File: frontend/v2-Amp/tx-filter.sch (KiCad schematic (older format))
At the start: 88 parts, among them K10 HK4100, K11 HK4100, K12 HK4100, K13 HK4100, K14 HK4100, K15 HK4100, K2 HK4100, K3 HK4100, K4 HK4100, K5 HK4100, K6 HK4100, K7 HK4100, K8 HK4100, K9 HK4100

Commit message: Starting V1.1 updates
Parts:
- added C2: 82pf, HERMESLITE:C_0805, symbol C
- added C3, C63: DNI, HERMESLITE:C_0805, symbol C
- added C4, C6: 150pf, HERMESLITE:C_0805, symbol C
- added C5: 56pf, HERMESLITE:C_0805, symbol C
- added C64: 82pF, HERMESLITE:C_0805, symbol C
- added L1, L22: 363nH, HERMESLITE:Choke_Toroid, symbol INDUCTOR
- added L2: 243nH, HERMESLITE:Choke_Toroid, symbol INDUCTOR
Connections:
- wire segments 147 -> 156
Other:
- note added: "11T T37-6\n7in #26"
- note added: "12/10M"
- note added: "12T T37-6\n8in #26"
- note added: "15T T37-6\n8in #26"
- note added: "16T T37-6\n9in #26"
- note added: "18T T37-6\n10in #26"
- note added: "19T T37-6\n11in #26"
- note added: "20T T37-6\n12in #26"
- note added: "23T T37-6\n13in #26"
- note added: "24T T37-2 \n14in #26"
- note added: "26T T37-2 \n15in #26"
- note added: "31T T37-2 \n17in #26"
- note added: "33T T37-2 \n18in #26"
- note added: "8T T37-6\n6in #26"
- note added: "9T T37-6\n7in #26"
- note removed: "12/10M and bypass"
- note removed: "12T T37-6\n #26"
- note removed: "14T T37-6\n #26"
- note removed: "16T T37-6\n #26"
- note removed: "17T T37-6\n #26"
- note removed: "19T T37-6\n #26"
- note removed: "20T T37-6\n #26"
- note removed: "21T T37-6\n #26"
- note removed: "25T T37-2 \n #28"
- note removed: "27T T37-2 \n #28"
- note removed: "30T T50-2 \n #30"
- note removed: "34T T50-2 \n #30"

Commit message: Filter updates
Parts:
- removed C2: 82pf, HERMESLITE:C_0805, symbol C
- removed C3, C63: DNI, HERMESLITE:C_0805, symbol C
- removed C4, C6: 150pf, HERMESLITE:C_0805, symbol C
- removed C5: 56pf, HERMESLITE:C_0805, symbol C
- removed C64: 82pF, HERMESLITE:C_0805, symbol C
- removed L1, L22: 363nH, HERMESLITE:Choke_Toroid, symbol INDUCTOR
- removed L2: 243nH, HERMESLITE:Choke_Toroid, symbol INDUCTOR
- C23: value 270pF -> 360pF
- C29: value DNI -> 100pf
- C41: value DNI -> 300pf
- C47: value 680pF -> 270pF
- C59: value 270pF -> 240pF
- L12: value 1.698uH -> 676nH
- L18: value 1.38uH -> 576nH
- L6: value 1.38uH -> 1.156uH
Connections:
- wire segments 156 -> 147
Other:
- note added: "12T T37-2\n8in #26"
- note added: "13T T37-2\n9in #26"
- note added: "17T T37-2\n11in #26"
- note removed: "12/10M"
- note removed: "20T T37-6\n12in #26"
- note removed: "23T T37-6\n13in #26"
- note removed: "8T T37-6\n6in #26"
- note removed: "9T T37-6\n7in #26"

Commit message: more changd for v2
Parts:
- C24: value 270pF -> 180pF
- C25, C61: value 180pF -> 100pF
- C30: value DNI -> 43pF
- C36: value 560pF -> 300pF
- C37, C49: value 390pF -> 270pF
- C42: value DNI -> 130pF
- C48: value 560pF -> 130pF
- C54: value DNI -> 0R Res
- C60: value 270pF -> DNI
- L13: value 1.257uH -> 455uH
- L14: value 904nH -> 668nH
- L19: value 1.09uH -> DNI
- L20, L8: value 773nH -> 548nH
- L7: value 1.09uH -> 642.5uH
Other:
- note added: "13T T37-6\n8in #26"
- note added: "15M"
- note added: "17M"
- note added: "30M/20M"
- note removed: "15T T37-6\n8in #26"
- note removed: "16T T37-6\n9in #26"
- note removed: "17/15M"
- note removed: "18T T37-6\n10in #26"
- note removed: "19T T37-6\n11in #26"
- note removed: "20M"
- note removed: "30M"

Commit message: v2rx changes and update to new kicad
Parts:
- C21, C22, C23, C24, C25, C26, C27, C28, C29, C30, C31, C32, C33, C34, C35, C36, C37, C38, C39, C40, C41, C42, C43, C44, C45, C46, C47, C48, C49, C50, C51, C52, C53, C54, C55, C56, C57, C58, C59, C60, C61, C62, C70, C71, C72, C73, C74, C75, C76, C77, C78, C79, C80, C81, C82, C83: symbol C -> C-RESCUE-amp

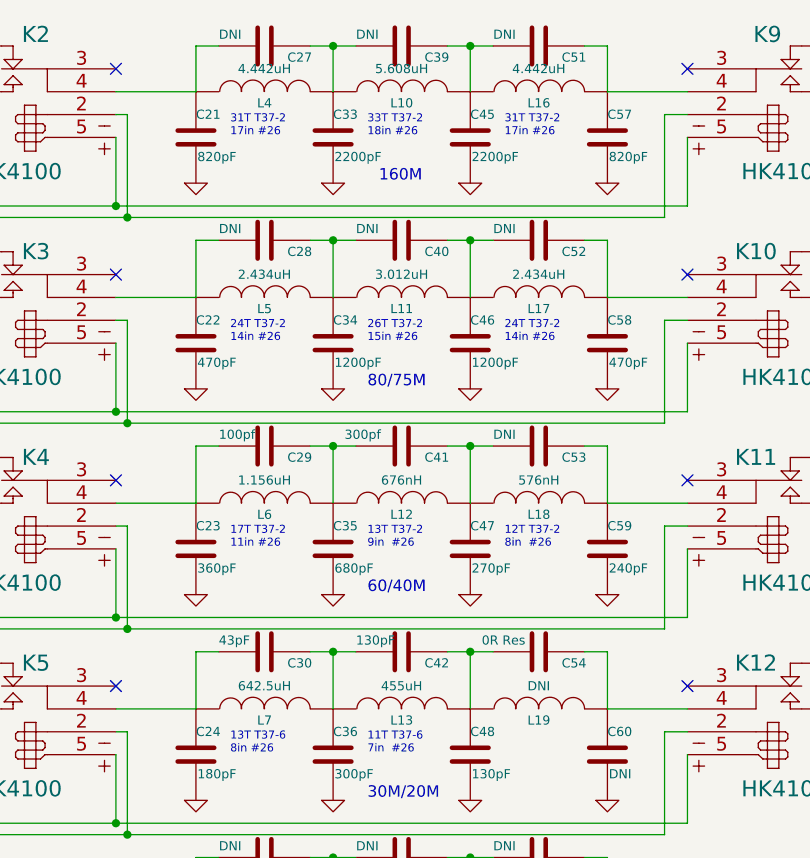
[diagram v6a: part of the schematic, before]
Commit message: Updates for v1.1 amp and V1.4 ADC
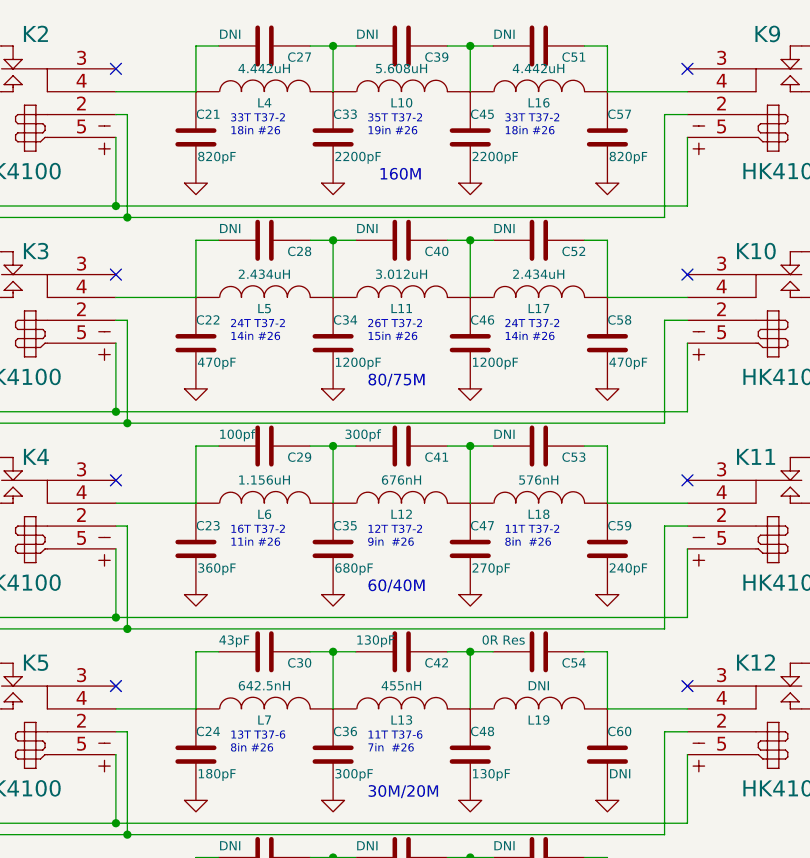
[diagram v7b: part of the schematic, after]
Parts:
- L13: value 455uH -> 455nH
- L7: value 642.5uH -> 642.5nH
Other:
- note added: "11T T37-2\n8in #26"
- note added: "12T T37-2\n9in #26"
- note added: "16T T37-2\n11in #26"
- note added: "35T T37-2 \n19in #26"
- note removed: "12T T37-2\n8in #26"
- note removed: "13T T37-2\n9in #26"
- note removed: "17T T37-2\n11in #26"
- note removed: "31T T37-2 \n17in #26"
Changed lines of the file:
@@
 P 3900 3500
 F 0 "L7" V 3850 3500 40  0000 C CNN
-F 1 "642.5uH" V 4000 3500 40  0000 C CNN
+F 1 "642.5nH" V 4000 3500 40  0000 C CNN
 F 2 "HERMESLITE:Choke_Toroid" H 3900 3500 60  0001 C CNN
 F 3 "" H 3900 3500 60  0000 C CNN
@@
 P 4500 3500
 F 0 "L13" V 4450 3500 40  0000 C CNN
-F 1 "455uH" V 4600 3500 40  0000 C CNN
+F 1 "455nH" V 4600 3500 40  0000 C CNN
 F 2 "HERMESLITE:Choke_Toroid" H 4500 3500 60  0001 C CNN
 F 3 "" H 4500 3500 60  0000 C CNN
@@
 15M
 Text Notes 3750 1000 0    35   ~ 0
-31T T37-2 \n17in #26
+33T T37-2 \n18in #26
 Text Notes 4950 1000 0    35   ~ 0
-31T T37-2 \n17in #26
+33T T37-2 \n18in #26
 Text Notes 4350 1000 0    35   ~ 0
-33T T37-2 \n18in #26
+35T T37-2 \n19in #26
 Text Notes 3750 1900 0    35   ~ 0
 24T T37-2 \n14in #26
@@
 24T T37-2 \n14in #26
 Text Notes 3750 2800 0    35   ~ 0
-17T T37-2\n11in #26
+16T T37-2\n11in #26
 Text Notes 4350 2800 0    35   ~ 0
-13T T37-2\n9in  #26
+12T T37-2\n9in  #26
 Text Notes 4950 2800 0    35   ~ 0
-12T T37-2\n8in  #26
+11T T37-2\n8in  #26
 Text Notes 3750 3700 0    35   ~ 0
 13T T37-6\n8in #26

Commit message: Ver 1.1 changes
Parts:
- added C2: 82pf, HERMESLITE:C_0805, symbol C-RESCUE-amp
- added C3, C63: DNI, HERMESLITE:C_0805, symbol C-RESCUE-amp
- added C4, C6: 150pf, HERMESLITE:C_0805, symbol C-RESCUE-amp
- added C5: 56pf, HERMESLITE:C_0805, symbol C-RESCUE-amp
- added C64: 82pF, HERMESLITE:C_0805, symbol C-RESCUE-amp
- added L1, L22: 363nH, Resistors_SMD:R_0805_HandSoldering, symbol INDUCTOR
- added L2: 243nH, Resistors_SMD:R_0805_HandSoldering, symbol INDUCTOR
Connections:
- net GND: now also C2.2, C4.2, C6.2, C64.2
- net at K8.4: now also C2.1, C3.2, L1.1; no longer K15.4
- new net: C63.1, C64.1, K15.4, L22.2
- new net: C3.1, C4.1, C5.2, L1.2, L2.1
- new net: C5.1, C6.1, C63.2, L2.2, L22.1
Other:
- note added: "8T T37-6\n6in #26"
- note added: "9T T37-6\n7in #26"
